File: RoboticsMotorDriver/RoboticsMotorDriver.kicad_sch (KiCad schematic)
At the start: 13 parts, among them J1 Screw_Terminal_01x02, Q1 IRLR8743TRPBF, Q2 IRLR8743TRPBF, Q3 IRLR8743TRPBF, Q4 IRLR8743TRPBF, U1 ATTINY424-XU, U2 AP7375-33SA-7

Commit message: Updated KiCAD schematic
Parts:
- added C2, C3: 10uF, symbol Device:C
- added C4, C5: 100nF, symbol Device:C
- added C6, C7: 1uF, symbol Device:C
- added D1, D2: D_Schottky, symbol Device:D_Schottky
- added U3, U4: HALF_BRIDGE_DRIVER_DGD2003, symbol SCM_LIB:HALF_BRIDGE_DRIVER_DGD2003
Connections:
- net +12V: now also C2.1
- net +5V: now also C3.1
- net GND: now also C2.2, C3.2, C4.1, C5.1, U3.4 (COM), U4.4 (COM)
- net at U1.11 (PA1): now also U4.3 (LIN)
- net at U1.12 (PA2): now also U4.2 (HIN)
- net at U1.13 (PA3EXTCLK): now also U3.3 (LIN)
- net at U1.9 (PB0): now also U3.2 (HIN)
- net DRIVER_HIGH renamed DRIVER_HIGH_0
- net DRIVER_HIGH_0: now also U3.7 (HO); no longer R5.2
- net DRIVER_LOW renamed DRIVER_HIGH_1
- net DRIVER_HIGH_1: now also U4.7 (HO); no longer R4.1
- new net: C6.1, D1.1 (K), U3.8 (VB)
- new net: C4.2, D1.2 (A), U3.1 (VCC)
- new net: C6.2, U3.6 (VS)
- new net: C5.2, D2.2 (A), U4.1 (VCC)
- new net: C7.2, U4.6 (VS)
- new net: C7.1, D2.1 (K), U4.8 (VB)
- new net DRIVER_LOW_0: R4.1, U3.5 (LO)
- new net DRIVER_LOW_1: R5.2, U4.5 (LO)
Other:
- moved on the sheet: J1, Q1, Q2, Q3, Q4, R2, R3, R4, R5

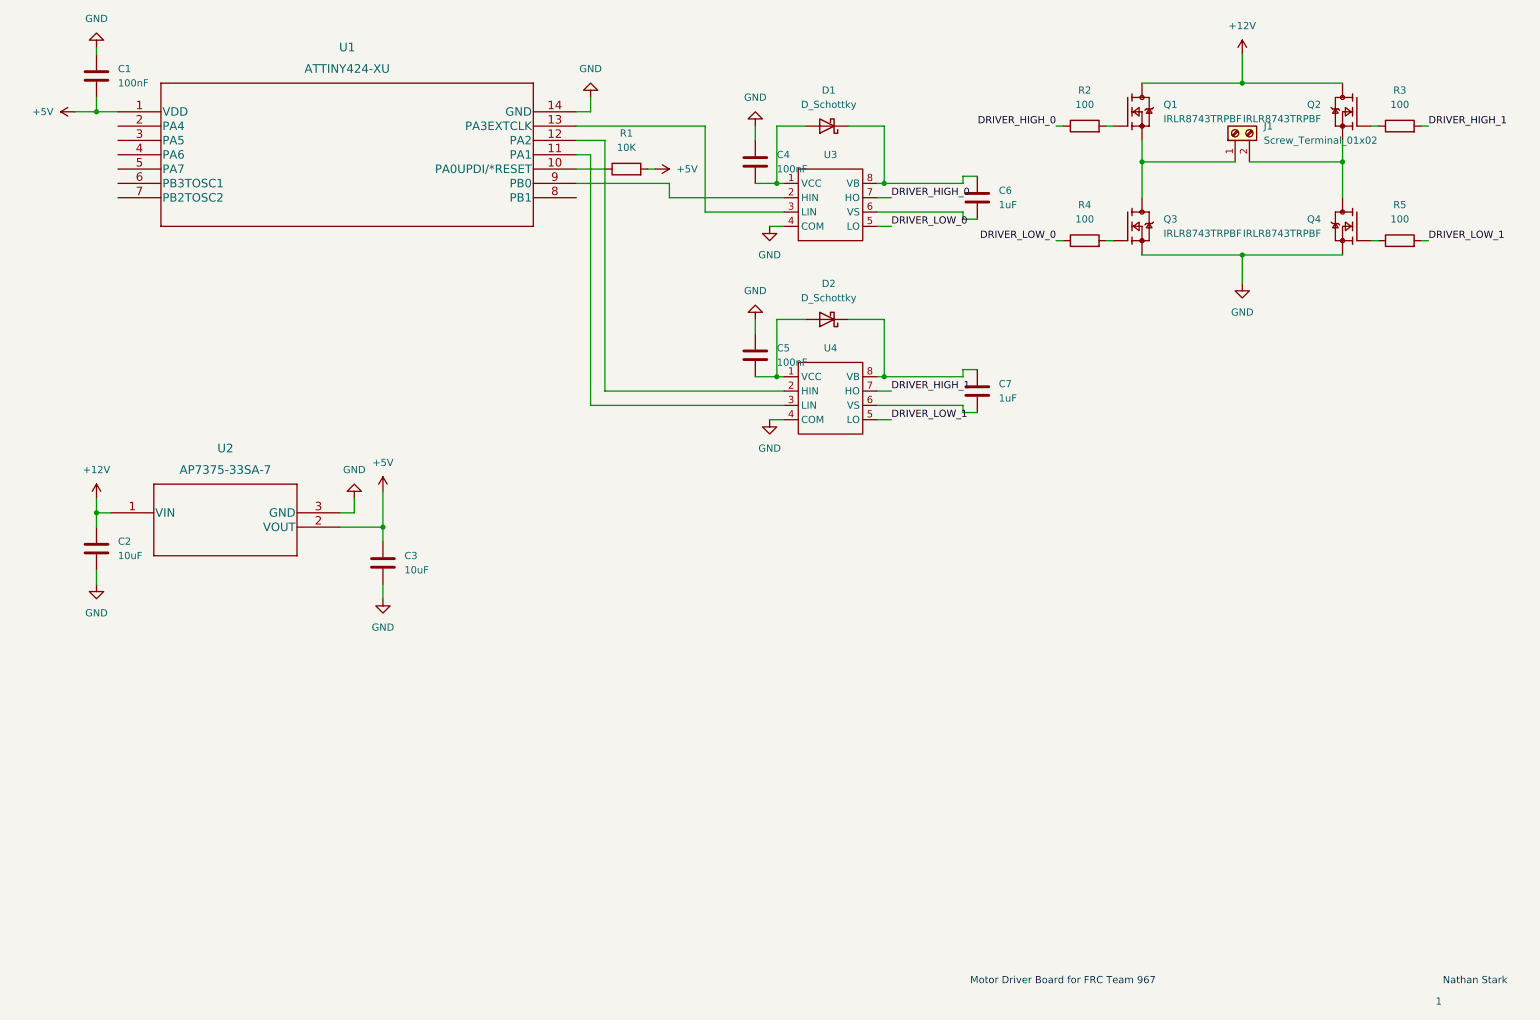
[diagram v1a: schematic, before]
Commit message: Added more components and fixed issues in schematic
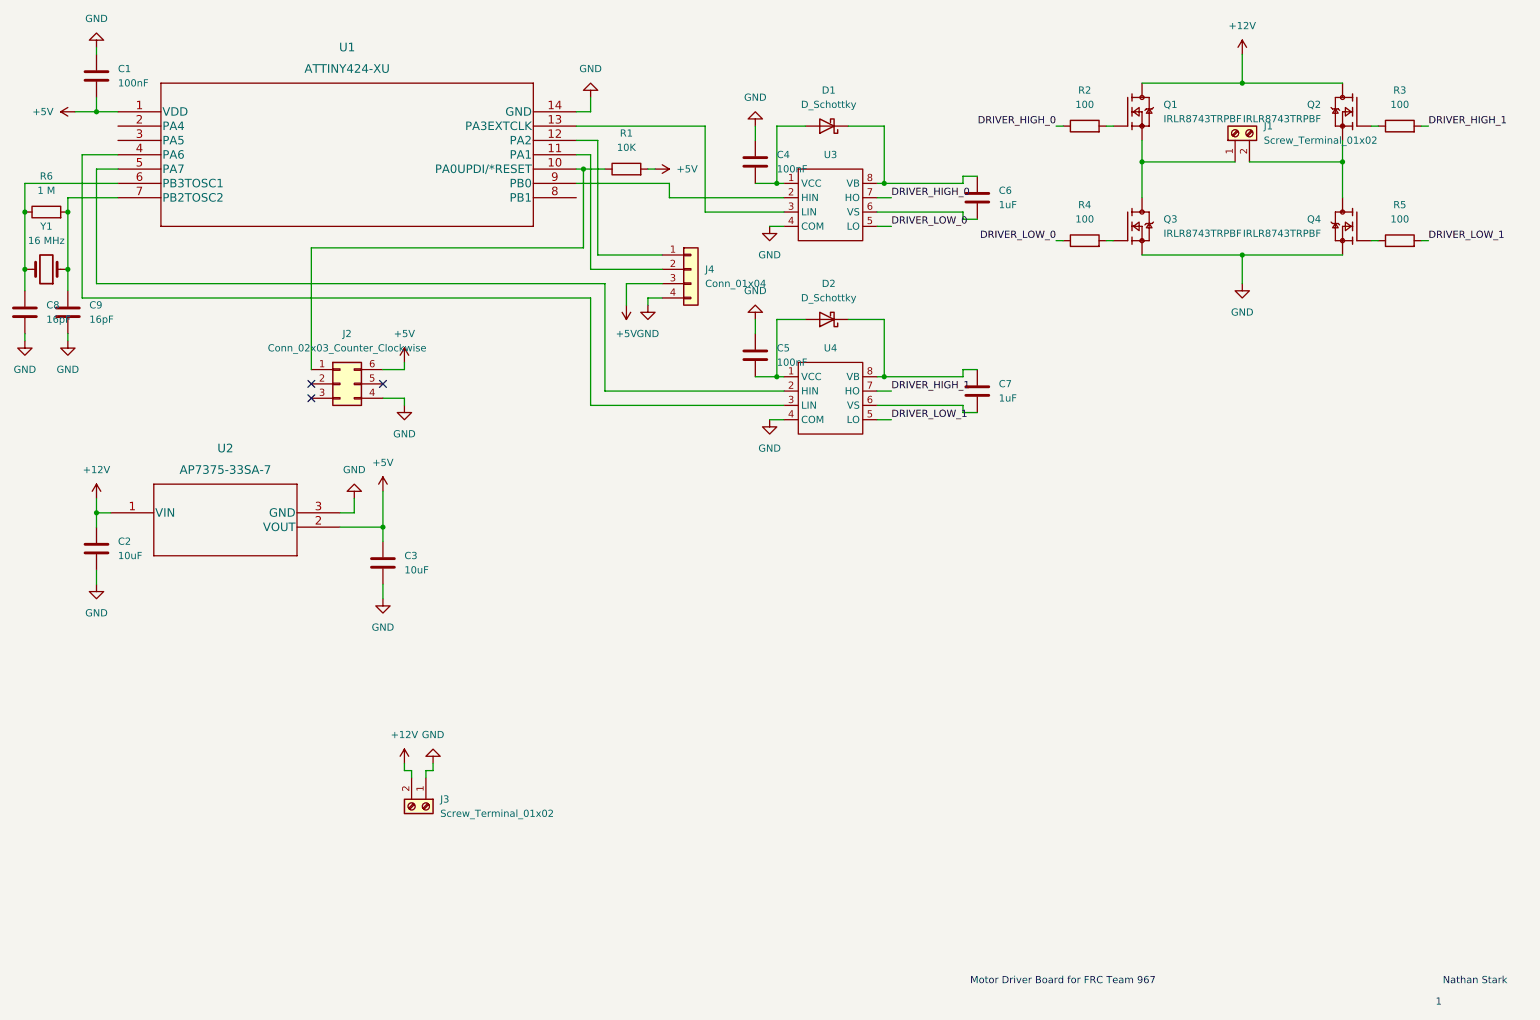
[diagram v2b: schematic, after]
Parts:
- added C8, C9: 16pF, Capacitor_SMD:C_0603_1608Metric, symbol Device:C
- added J2: Conn_02x03_Counter_Clockwise, Connector_PinHeader_2.54mm:PinHeader_2x03_P2.54mm_Vertical, symbol Connector_Generic:Conn_02x03_Counter_Clockwise
- added J3: Screw_Terminal_01x02, TerminalBlock:TerminalBlock_bornier-2_P5.08mm, symbol Connector:Screw_Terminal_01x02
- added J4: Conn_01x04, Connector_PinHeader_2.54mm:PinHeader_1x04_P2.54mm_Vertical, symbol Connector_Generic:Conn_01x04
- added R6: 1 M, Resistor_SMD:R_0603_1608Metric, symbol Device:R
- added Y1: 16 MHz, Crystal:Crystal_SMD_5032-2Pin_5.0x3.2mm, symbol Device:Crystal
- C1, C2, C3, C4, C5, C6, C7: footprint (none) -> Capacitor_SMD:C_0603_1608Metric
- D1, D2: footprint (none) -> Diode_SMD:D_2114_3652Metric
- J1: footprint (none) -> TerminalBlock:TerminalBlock_bornier-2_P5.08mm
- R1, R2, R3, R4, R5: footprint (none) -> Resistor_SMD:R_0603_1608Metric
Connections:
- net +12V: now also J3.2 (Pin_2)
- net +5V: now also J2.6 (Pin_6), J4.3 (Pin_3)
- net GND: now also C8.2, C9.2, J2.4 (Pin_4), J3.1 (Pin_1), J4.4 (Pin_4)
- net at U4.2 (HIN): now also U1.5 (PA7); no longer U1.12 (PA2)
- net at U4.3 (LIN): now also U1.4 (PA6); no longer U1.11 (PA1)
- net at R1.1, U1.10 (PA0UPDI/*RESET): now also J2.1 (Pin_1)
- net at U1.6 (PB3TOSC1): now also C8.1, R6.1, Y1.2
- net at U1.7 (PB2TOSC2): now also C9.1, R6.2, Y1.1
- new net: J4.1 (Pin_1), U1.12 (PA2)
- new net: J4.2 (Pin_2), U1.11 (PA1)
- no-connect marks 0 -> 3
